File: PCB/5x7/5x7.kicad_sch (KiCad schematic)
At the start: 49 parts, among them J1 Conn_01x03, J2 Conn_01x03

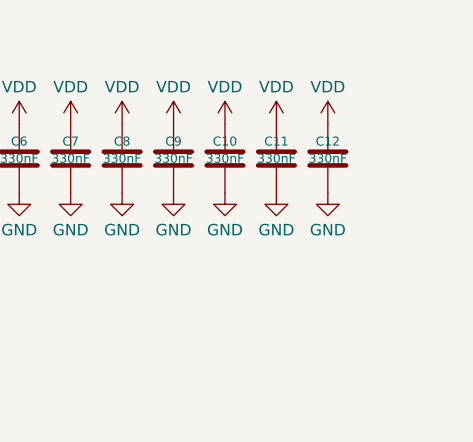
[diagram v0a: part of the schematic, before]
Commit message: Reworked for orientation, and ordered
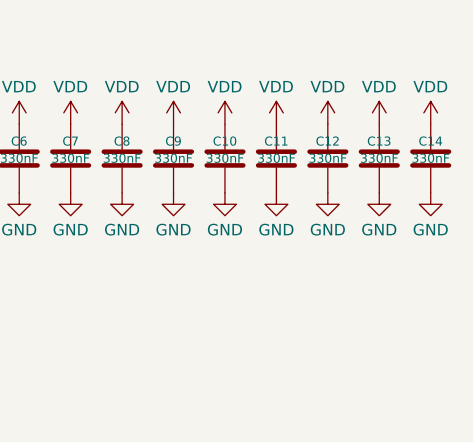
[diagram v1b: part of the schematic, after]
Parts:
- added C13, C14: 330nF, RevK:C_0402, symbol Device:C
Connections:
- net GND: now also C13.2, C14.2
- net VDD: now also C13.1, C14.1
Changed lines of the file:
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@@
+    )
+  )
+  (symbol (lib_id "power:VDD") (at 172.72 33.655 0) (unit 1)
+    (in_bom yes) (on_board yes) (dnp no) (fields_autoplaced)
+    (property "Reference" "#PWR095" (at 172.72 37.465 0)
+      (effects (font (size 1.27 1.27)) hide)
+    )
+    (property "Value" "VDD" (at 172.72 29.5219 0)
+      (effects (font (size 1.27 1.27)))
+    )
+    (property "Footprint" "" (at 172.72 33.655 0)
+      (effects (font (size 1.27 1.27)) hide)
+    )
+    (property "Datasheet" "" (at 172.72 33.655 0)
+      (effects (font (size 1.27 1.27)) hide)
+    )
+    (pin "1")
+    (instances
+      (project "5x7"
+        (path "/46c350bb-7de4-4e81-aafd-4af55e37aab0"
+          (reference "#PWR095") (unit 1)
+        )
+      )
     )
   )
@@
     )
   )
+  (symbol (lib_id "power:GND") (at 178.435 41.275 0) (unit 1)
+    (in_bom yes) (on_board yes) (dnp no) (fields_autoplaced)
+    (property "Reference" "#PWR098" (at 178.435 47.625 0)
+      (effects (font (size 1.27 1.27)) hide)
+    )
+    (property "Value" "GND" (at 178.435 45.4081 0)
+      (effects (font (size 1.27 1.27)))
+    )
+    (property "Footprint" "" (at 178.435 41.275 0)
+      (effects (font (size 1.27 1.27)) hide)
+    )
+    (property "Datasheet" "" (at 178.435 41.275 0)
+      (effects (font (size 1.27 1.27)) hide)
+    )
+    (pin "1")
+    (instances
+      (project "5x7"
+        (path "/46c350bb-7de4-4e81-aafd-4af55e37aab0"
+          (reference "#PWR098") (unit 1)
+        )
+      )
+    )
+  )
   (symbol (lib_id "power:VDD") (at 35.56 93.98 0) (unit 1)
     (in_bom yes) (on_board yes) (dnp no) (fields_autoplaced)
@@
     )
   )
+  (symbol (lib_id "power:VDD") (at 178.435 33.655 0) (unit 1)
+    (in_bom yes) (on_board yes) (dnp no) (fields_autoplaced)
+    (property "Reference" "#PWR097" (at 178.435 37.465 0)
+      (effects (font (size 1.27 1.27)) hide)
+    )
+    (property "Value" "VDD" (at 178.435 29.5219 0)
+      (effects (font (size 1.27 1.27)))
+    )
+    (property "Footprint" "" (at 178.435 33.655 0)
+      (effects (font (size 1.27 1.27)) hide)
+    )
+    (property "Datasheet" "" (at 178.435 33.655 0)
+      (effects (font (size 1.27 1.27)) hide)
+    )
+    (pin "1")
+    (instances
+      (project "5x7"
+        (path "/46c350bb-7de4-4e81-aafd-4af55e37aab0"
+          (reference "#PWR097") (unit 1)
+        )
+      )
+    )
+  )
   (symbol (lib_id "power:GND") (at 43.18 146.05 0) (unit 1)
     (in_bom yes) (on_board yes) (dnp no) (fields_autoplaced)
@@
         (path "/46c350bb-7de4-4e81-aafd-4af55e37aab0"
           (reference "D35") (unit 1)
+        )
+      )
+    )
+  )
+  (symbol (lib_id "Device:C") (at 178.435 37.465 0) (unit 1)
+    (in_bom yes) (on_board yes) (dnp no)
+    (property "Reference" "C14" (at 178.435 35.56 0)
+      (effects (font (size 1 1)))
+    )
+    (property "Value" "330nF" (at 178.435 37.465 0)
+      (effects (font (size 1 1)))
+    )
+    (property "Footprint" "RevK:C_0402" (at 179.4002 41.275 0)
+      (effects (font (size 1.27 1.27)) hide)
+    )
+    (property "Datasheet" "~" (at 178.435 37.465 0)
+      (effects (font (size 1.27 1.27)) hide)
+    )
+    (pin "1")
+    (pin "2")
+    (instances
+      (project "5x7"
+        (path "/46c350bb-7de4-4e81-aafd-4af55e37aab0"
+          (reference "C14") (unit 1)
         )
       )
@@
     )
   )
+  (symbol (lib_id "Device:C") (at 172.72 37.465 0) (unit 1)
+    (in_bom yes) (on_board yes) (dnp no)
+    (property "Reference" "C13" (at 172.72 35.56 0)
+      (effects (font (size 1 1)))
+    )
+    (property "Value" "330nF" (at 172.72 37.465 0)
+      (effects (font (size 1 1)))
+    )
+    (property "Footprint" "RevK:C_0402" (at 173.6852 41.275 0)
+      (effects (font (size 1.27 1.27)) hide)
+    )
+    (property "Datasheet" "~" (at 172.72 37.465 0)
+      (effects (font (size 1.27 1.27)) hide)
+    )
+    (pin "1")
+    (pin "2")
+    (instances
+      (project "5x7"
+        (path "/46c350bb-7de4-4e81-aafd-4af55e37aab0"
+          (reference "C13") (unit 1)
+        )
+      )
+    )
+  )
   (symbol (lib_id "power:GND") (at 132.715 41.275 0) (unit 1)
     (in_bom yes) (on_board yes) (dnp no) (fields_autoplaced)
@@
         )
       )
+    )
+  )
+  (symbol (lib_id "power:GND") (at 172.72 41.275 0) (unit 1)
+    (in_bom yes) (on_board yes) (dnp no) (fields_autoplaced)
+    (property "Reference" "#PWR096" (at 172.72 47.625 0)
+      (effects (font (size 1.27 1.27)) hide)
+    )
+    (property "Value" "GND" (at 172.72 45.4081 0)
+      (effects (font (size 1.27 1.27)))
+    )
+    (property "Footprint" "" (at 172.72 41.275 0)
+      (effects (font (size 1.27 1.27)) hide)
+    )
+    (property "Datasheet" "" (at 172.72 41.275 0)
+      (effects (font (size 1.27 1.27)) hide)
+    )
+    (pin "1")
+    (instances
+      (project "5x7"
+        (path "/46c350bb-7de4-4e81-aafd-4af55e37aab0"
+          (reference "#PWR096") (unit 1)
+        )
+      )

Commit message: Comment
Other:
- note added: "Rework for caps and vias at top/bottom"
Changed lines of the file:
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@@
     (stroke (width 0) (type default))
+  )
+  (text "Rework for caps and vias at top/bottom" (at 96.52 93.98 0)
+    (effects (font (size 5 5)) (justify left bottom))
   )
   (symbol (lib_id "power:GND") (at 50.8 168.275 0) (unit 1)

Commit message: Comment
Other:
- note added: "Rework for caps and vias at top/bottom Maybe long strip 8 picels high to allow scrolling text"
- note removed: "Rework for caps and vias at top/bottom"
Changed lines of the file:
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@@
     (stroke (width 0) (type default))
   )
-  (text "Rework for caps and vias at top/bottom" (at 96.52 93.98 0)
+  (text "Rework for caps and vias at top/bottom\nMaybe long strip 8 picels high to allow scrolling text"
+    (at 96.52 93.98 0)
     (effects (font (size 5 5)) (justify left bottom))
   )

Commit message: New layout
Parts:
- removed C11, C12, C13, C14: 330nF, RevK:C_0402, symbol Device:C
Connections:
- net VDD renamed VCC
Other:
- note removed: "Rework for caps and vias at top/bottom Maybe long strip 8 picels high to allow scrolling text"
- moved on the sheet: C1, C2, D1, D2, D3, D4, D5, J1, J2

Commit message: PCB Update
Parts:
- D1, D10, D11, D12, D13, D14, D15, D16, D17, D18, D19, D2, D20, D21, D22, D23, D24, D25, D26, D27, D28, D29, D3, D30, D31, D32, D33, D34, D35, D4, D5, D6, D7, D8, D9: LCSC Part # C5349953 -> (none); MPN (none) -> C5349953
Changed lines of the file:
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@@
 			)
 		)
-		(property "LCSC Part #" "C5349953"
+		(property "MPN" "C5349953"
 			(at 98.425 109.22 0)
 			(effects
@@
 			)
 		)
-		(property "LCSC Part #" "C5349953"
+		(property "MPN" "C5349953"
 			(at 113.03 86.36 0)
 			(effects
@@
 			)
 		)
-		(property "LCSC Part #" "C5349953"
+		(property "MPN" "C5349953"
 			(at 83.82 124.46 0)
 			(effects
@@
 			)
 		)
-		(property "LCSC Part #" "C5349953"
+		(property "MPN" "C5349953"
 			(at 113.03 116.84 0)
 			(effects
@@
 			)
 		)
-		(property "LCSC Part #" "C5349953"
+		(property "MPN" "C5349953"
 			(at 54.61 78.74 0)
 			(effects
@@
 			)
 		)
-		(property "LCSC Part #" "C5349953"
+		(property "MPN" "C5349953"
 			(at 69.215 93.98 0)
 			(effects
@@
 			)
 		)
-		(property "LCSC Part #" "C5349953"
+		(property "MPN" "C5349953"
 			(at 69.215 116.84 0)
 			(effects
@@
 			)
 		)
-		(property "LCSC Part #" "C5349953"
+		(property "MPN" "C5349953"
 			(at 98.425 116.84 0)
 			(effects
@@
 			)
 		)
-		(property "LCSC Part #" "C5349953"
+		(property "MPN" "C5349953"
 			(at 83.82 93.98 0)
 			(effects
@@
 			)
 		)
-		(property "LCSC Part #" "C5349953"
+		(property "MPN" "C5349953"
 			(at 83.82 109.22 0)
 			(effects
@@
 			)
 		)
-		(property "LCSC Part #" "C5349953"
+		(property "MPN" "C5349953"
 			(at 113.03 93.98 0)
 			(effects
@@
 			)
 		)
-		(property "LCSC Part #" "C5349953"
+		(property "MPN" "C5349953"
 			(at 113.03 124.46 0)
 			(effects
@@
 			)
 		)
-		(property "LCSC Part #" "C5349953"
+		(property "MPN" "C5349953"
 			(at 83.82 101.6 0)
 			(effects
@@
 			)
 		)
-		(property "LCSC Part #" "C5349953"
+		(property "MPN" "C5349953"
 			(at 98.425 93.98 0)
 			(effects
@@
 			)
 		)
-		(property "LCSC Part #" "C5349953"
+		(property "MPN" "C5349953"
 			(at 98.425 101.6 0)
 			(effects
@@
 			)
 		)
-		(property "LCSC Part #" "C5349953"
+		(property "MPN" "C5349953"
 			(at 54.61 116.84 0)
 			(effects
@@
 			)
 		)
-		(property "LCSC Part #" "C5349953"
+		(property "MPN" "C5349953"
 			(at 113.03 109.22 0)
 			(effects
@@
 			)
 		)
-		(property "LCSC Part #" "C5349953"
+		(property "MPN" "C5349953"
 			(at 69.215 78.74 0)
 			(effects
@@
 			)
 		)
-		(property "LCSC Part #" "C5349953"
+		(property "MPN" "C5349953"
 			(at 113.03 78.74 0)
 			(effects
@@
 			)
 		)
-		(property "LCSC Part #" "C5349953"
+		(property "MPN" "C5349953"
 			(at 83.82 116.84 0)
 			(effects
@@
 			)
 		)
-		(property "LCSC Part #" "C5349953"
+		(property "MPN" "C5349953"
 			(at 98.425 78.74 0)
 			(effects
@@
 			)
 		)
-		(property "LCSC Part #" "C5349953"
+		(property "MPN" "C5349953"
 			(at 54.61 109.22 0)
 			(effects
@@
 			)
 		)
-		(property "LCSC Part #" "C5349953"
+		(property "MPN" "C5349953"
 			(at 69.215 86.36 0)
 			(effects
@@
 			)
 		)
-		(property "LCSC Part #" "C5349953"
+		(property "MPN" "C5349953"
 			(at 69.215 124.46 0)
 			(effects
@@
 			)
 		)
-		(property "LCSC Part #" "C5349953"
+		(property "MPN" "C5349953"
 			(at 98.425 86.36 0)
 			(effects
@@
 			)
 		)
-		(property "LCSC Part #" "C5349953"
+		(property "MPN" "C5349953"
 			(at 54.61 101.6 0)
 			(effects
@@
 			)
 		)
-		(property "LCSC Part #" "C5349953"
+		(property "MPN" "C5349953"
 			(at 98.425 124.46 0)
 			(effects
@@
 			)
 		)
-		(property "LCSC Part #" "C5349953"
+		(property "MPN" "C5349953"
 			(at 54.61 86.36 0)
 			(effects
@@
 			)
 		)
-		(property "LCSC Part #" "C5349953"
+		(property "MPN" "C5349953"
 			(at 83.82 78.74 0)
 			(effects
@@
 			)
 		)
-		(property "LCSC Part #" "C5349953"
+		(property "MPN" "C5349953"
 			(at 54.61 124.46 0)
 			(effects
@@
 			)
 		)
-		(property "LCSC Part #" "C5349953"
+		(property "MPN" "C5349953"
 			(at 69.215 101.6 0)
 			(effects
@@
 			)
 		)
-		(property "LCSC Part #" "C5349953"
+		(property "MPN" "C5349953"
 			(at 83.82 86.36 0)
 			(effects
@@
 			)
 		)
-		(property "LCSC Part #" "C5349953"
+		(property "MPN" "C5349953"
 			(at 113.03 101.6 0)
 			(effects
@@
 			)
 		)
-		(property "LCSC Part #" "C5349953"
+		(property "MPN" "C5349953"
 			(at 69.215 109.22 0)
 			(effects
@@
 			)
 		)
-		(property "LCSC Part #" "C5349953"
+		(property "MPN" "C5349953"
 			(at 54.61 93.98 0)
 			(effects
